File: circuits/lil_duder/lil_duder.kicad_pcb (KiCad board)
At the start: 2 copper layers, 64 x 65 mm, 51 parts, among them J1 Mic+, J10 GND_Conn, J11 RST+, J12 RST-, J13 LED4, J14 A1, J2 Mic-, J3 LED1, J4 LED2, J5 SPK_A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

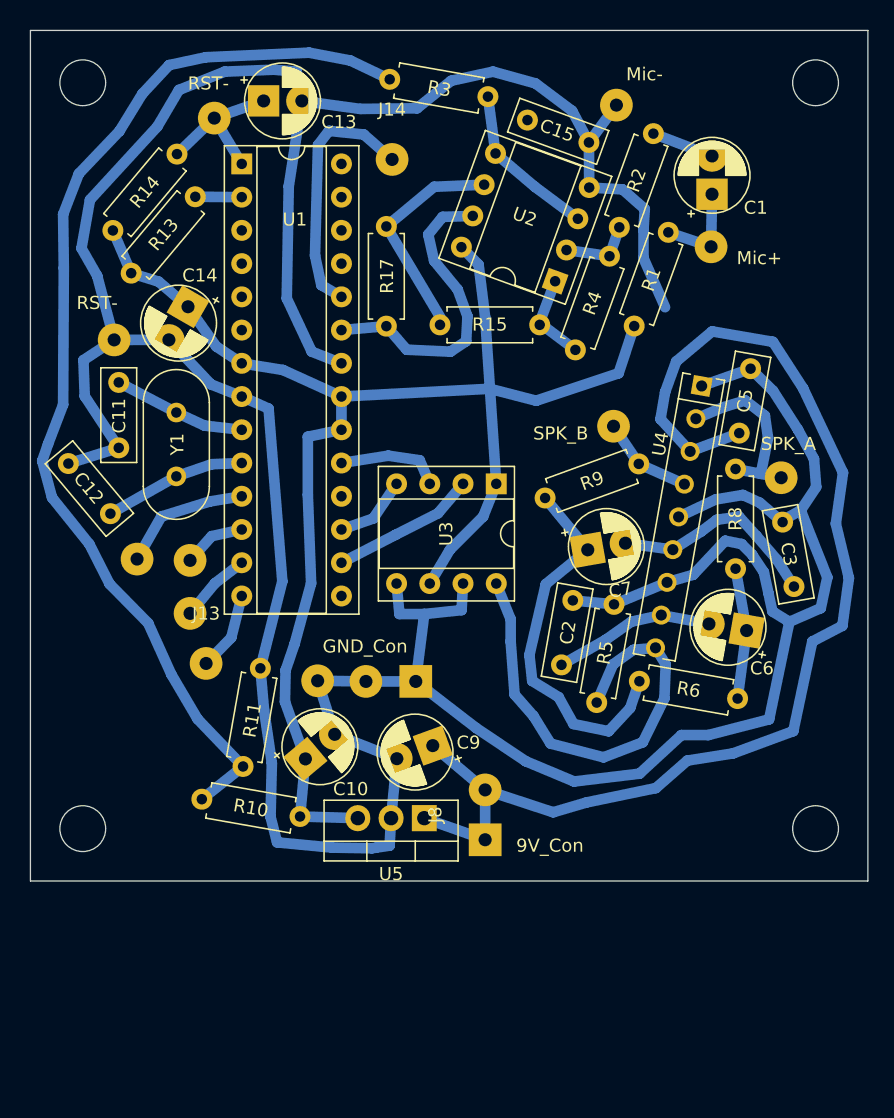
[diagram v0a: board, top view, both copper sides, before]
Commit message: switched power to 5v for speaker driver
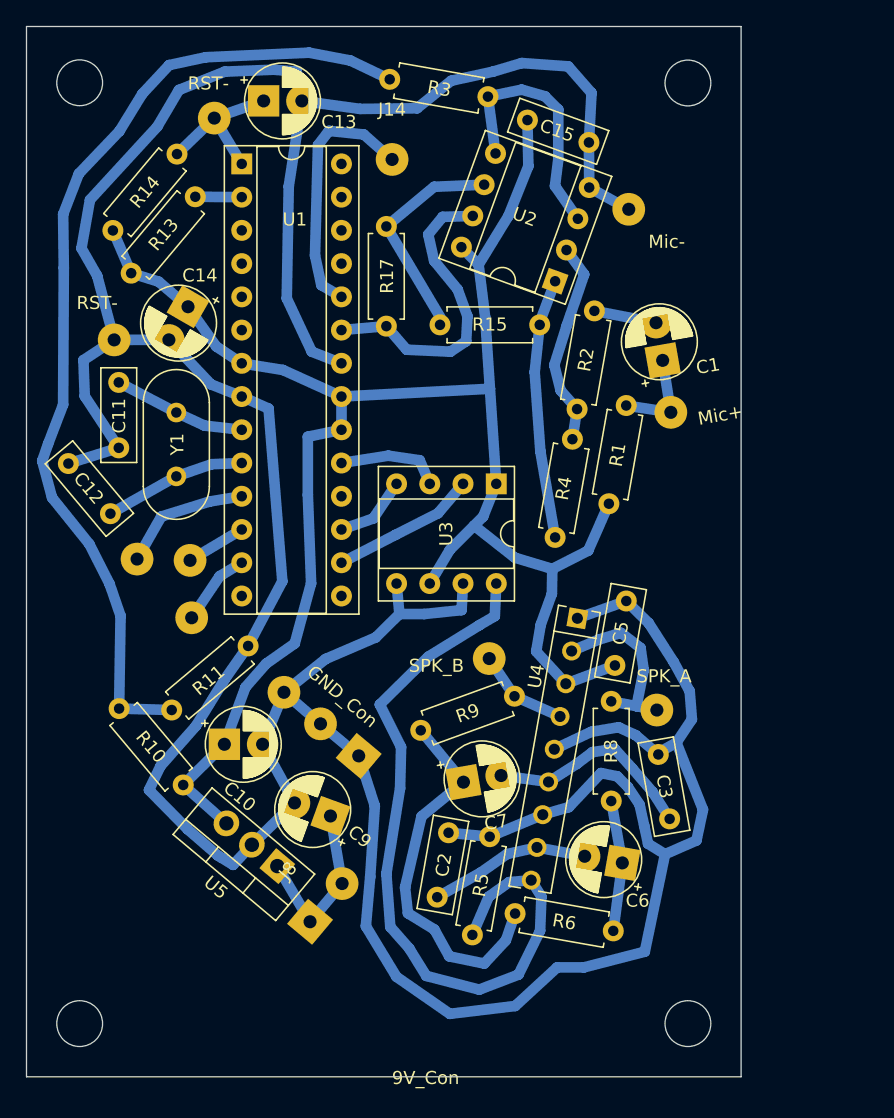
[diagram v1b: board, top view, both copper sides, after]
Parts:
- removed J13: LED4, Connector_Wire:SolderWirePad_1x01_Drill1mm
- removed the REF** at (73.0, 74.0)
- removed the REF** at (73.0, 17.0)
- added REF**: MountingHole_3.5mm, MountingHole:MountingHole_3.5mm, F.Cu at (63.2, 17.0)
- added REF**: MountingHole_3.5mm, MountingHole:MountingHole_3.5mm, F.Cu at (16.8, 88.9)
- moved REF** 48.6 mm to (63.2, 88.9)
- moved C5 20.1 mm to (57.7, 61.5)
- moved C7 20.1 mm to (48.0, 70.9)
- moved J5 20.1 mm to (60.9, 64.9)
- moved R5 20.1 mm to (48.1, 74.6)
- moved R6 20.1 mm to (57.5, 81.8)
- moved C2 20.1 mm to (44.1, 79.2)
- moved C6 20.1 mm to (56.6, 75.5)
- moved J6 20.1 mm to (48.1, 61.0)
- moved R8 20.1 mm to (57.4, 64.3)
- moved R9 20.1 mm to (50.0, 63.9)
- moved U4 20.1 mm to (54.8, 57.9)
- moved C3 20.1 mm to (61.9, 73.3)
- moved J8 14.8 mm to (34.4, 81.1), turned to 50 degrees
- moved R4 14.4 mm to (53.1, 51.7), turned to 80 degrees
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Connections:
- C5 pad 1: +9V -> +5V
- U4 pad 3: +9V -> +5V
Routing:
- net +9V: track 92.3 -> 14.0 mm
- net +5V: track 115.5 -> 141.7 mm
- net Net-(R5-Pad2): track 35.4 -> 57.8 mm
- net Net-(R15-Pad2): track 6.83 -> 19.8 mm
- net Net-(R2-Pad1): track 5.65 -> 15.8 mm
- net +2V5: track 83.0 -> 75.2 mm
- net Net-(R3-Pad1): track 12.4 -> 19.2 mm
- net Net-(J13-Pad1): track 6.04 -> 0.00 mm
- net Earth: track 306.6 -> 309.2 mm
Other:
- board size 64 x 65 mm -> 54.6 x 80.3 mm

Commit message: changes to circuit
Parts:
- removed R15: 10k, Resistor_THT:R_Axial_DIN0207_L6.3mm_D2.5mm_P7.62mm_Horizontal
- removed R17: 100k, Resistor_THT:R_Axial_DIN0207_L6.3mm_D2.5mm_P7.62mm_Horizontal
- added REF**: SolderWirePad_1x01_Drill0.8mm, Connector_Wire:SolderWirePad_1x01_Drill0.8mm, F.Cu at (49.0, 37.8)
- added REF**: SolderWirePad_1x01_Drill0.8mm, Connector_Wire:SolderWirePad_1x01_Drill0.8mm, F.Cu at (40.6, 36.1)
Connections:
- R4 pad 1: Net-(R15-Pad2) -> Net-(R4-Pad1)
- U1 pad 23: Net-(R17-Pad1) -> Net-(R4-Pad1)
- U2 pad 1: Net-(R15-Pad2) -> Net-(R4-Pad1)
- U2 pad 5: Net-(R3-Pad1) -> Earth
- U2 pad 6: Net-(R15-Pad1) -> Net-(U2-Pad6)
- U2 pad 7: Net-(R17-Pad1) -> Net-(U2-Pad6)
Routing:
- net Net-(R4-Pad1): track 0.00 -> 34.9 mm
- net Net-(R17-Pad1): track 23.6 -> 0.00 mm
- net Net-(R15-Pad2): track 19.8 -> 0.00 mm
- net Net-(R15-Pad1): track 17.1 -> 0.00 mm
- net Earth: track 309.2 -> 315.8 mm
- net Net-(R3-Pad1): track 19.2 -> 14.8 mm
- net Net-(U2-Pad6): track 0.00 -> 2.54 mm
- net +5V: track 141.7 -> 140.8 mm
